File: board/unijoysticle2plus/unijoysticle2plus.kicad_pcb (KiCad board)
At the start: 2 copper layers, 4 parts, among them J1 DB9_Female, J2 DB9_Female, J4 Conn_01x02_Male, U1 ESP32-WROOM-32D

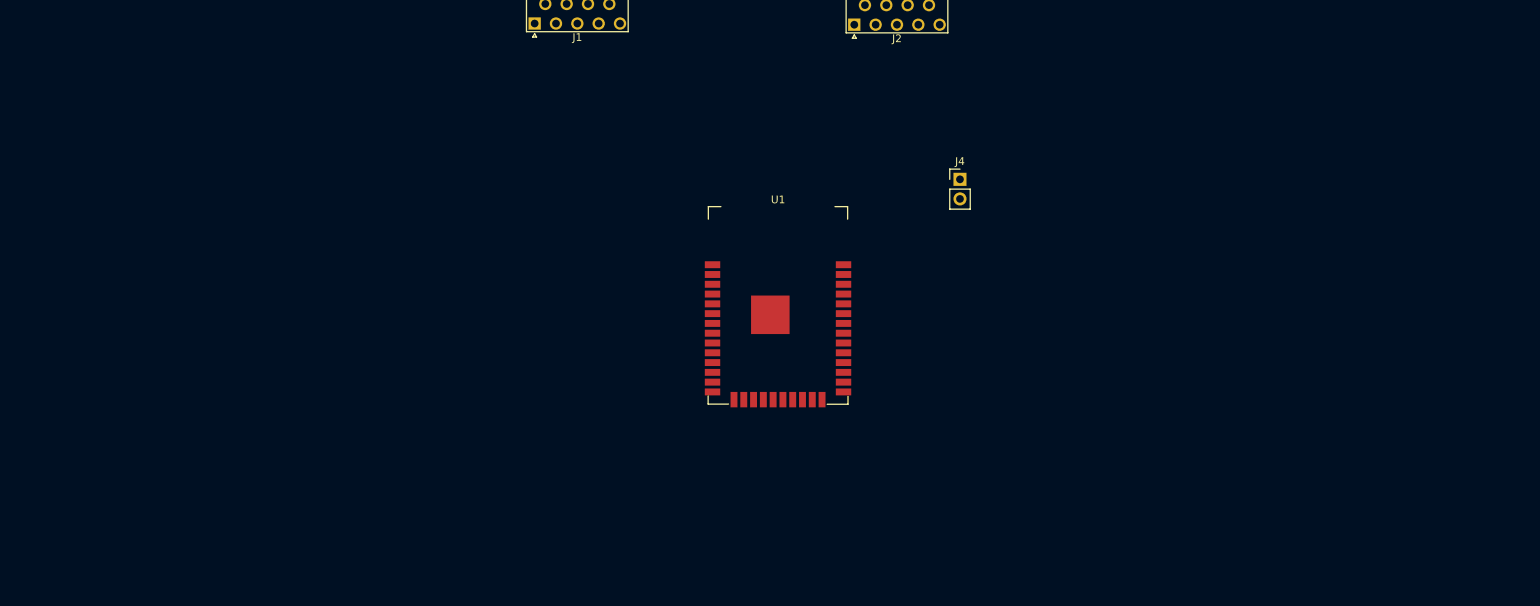
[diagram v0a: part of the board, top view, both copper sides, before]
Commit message: unijoysticle2plus: add some footprints
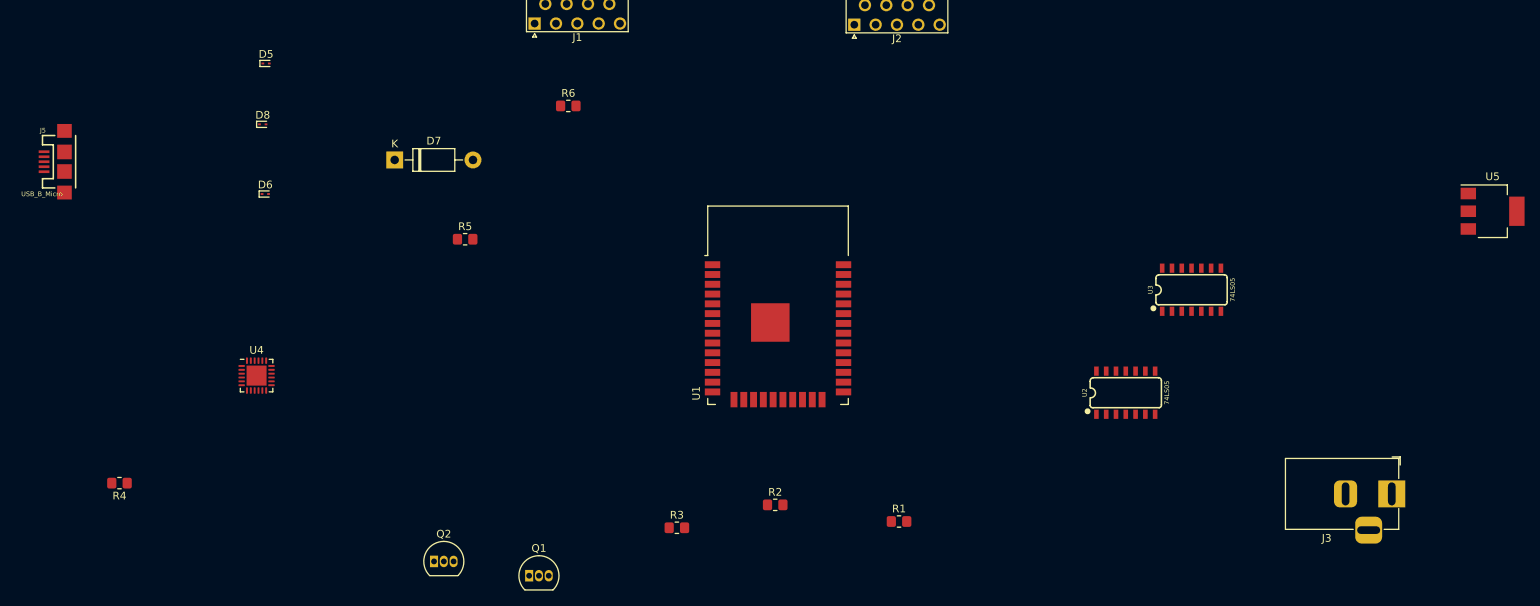
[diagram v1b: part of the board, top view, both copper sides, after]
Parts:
- removed J4: Conn_01x02_Male, Connector_PinHeader_2.54mm:PinHeader_1x02_P2.54mm_Vertical
- added D5: ESD9B5.0ST5G, Diode_SMD:D_SOD-923, F.Cu at (109.9, 81.0)
- added D6: ESD9B5.0ST5G, Diode_SMD:D_SOD-923, F.Cu at (109.8, 98.0)
- added D7: 1N5819, Diode_THT:D_DO-41_SOD81_P10.16mm_Horizontal, F.Cu at (126.5, 93.5)
- added D8: ESD9B5.0ST5G, Diode_SMD:D_SOD-923, F.Cu at (109.4, 88.9)
- added J3: Barrel_Jack, Connector_BarrelJack:BarrelJack_Horizontal, F.Cu at (255.9, 136.9)
- added J5: USB_B_Micro, Connectors:USB-MICROB, F.Cu at (83.7, 93.8)
- added Q1: S8050, Package_TO_SOT_THT:TO-92_Inline, F.Cu at (144.0, 147.5)
- added Q2: S8050, Package_TO_SOT_THT:TO-92_Inline, F.Cu at (131.6, 145.6)
- added R1: 150, Resistor_SMD:R_0805_2012Metric_Pad1.20x1.40mm_HandSolder, F.Cu at (192.0, 140.5)
- added R2: 150, Resistor_SMD:R_0805_2012Metric_Pad1.20x1.40mm_HandSolder, F.Cu at (175.9, 138.3)
- added R3: 10k, Resistor_SMD:R_0805_2012Metric_Pad1.20x1.40mm_HandSolder, F.Cu at (163.2, 141.3)
- added R4: 1k, Resistor_SMD:R_0805_2012Metric_Pad1.20x1.40mm_HandSolder, F.Cu at (90.8, 135.5)
- added R5: 10k, Resistor_SMD:R_0805_2012Metric_Pad1.20x1.40mm_HandSolder, F.Cu at (135.7, 103.8)
- added R6: 10k, Resistor_SMD:R_0805_2012Metric_Pad1.20x1.40mm_HandSolder, F.Cu at (149.1, 86.5)
- added U2: 74LS05, Silicon-Standard:SO14, F.Cu at (220.8, 123.7)
- added U3: 74LS05, Silicon-Standard:SO14, F.Cu at (229.3, 110.4)
- added U4: CP2102N-A01-GQFN24, Package_DFN_QFN:QFN-24-1EP_4x4mm_P0.5mm_EP2.6x2.6mm, F.Cu at (108.6, 121.5)
- added U5: AP2114H-3_3TRG1, Package_TO_SOT_SMD:SOT-223, F.Cu at (269.0, 100.2)
- U1: footprint digikey-footprints:ESP32-WROOM-32D -> RF_Module:ESP32-WROOM-32
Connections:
- net +5V renamed VDD
- J1 pad 1: (no net) -> /J1_UP
- J1 pad 2: (no net) -> /J1_DOWN
- J1 pad 3: (no net) -> /J1_LEFT
- J1 pad 4: (no net) -> /J1_RIGHT
- J1 pad 6: (no net) -> /J1_FIRE
- J2 pad 1: (no net) -> /J2_UP
- J2 pad 2: (no net) -> /J2_DOWN
- J2 pad 3: (no net) -> /J2_LEFT
- J2 pad 4: (no net) -> /J2_RIGHT
- J2 pad 6: (no net) -> /J2_FIRE
- U1 pad 10: (no net) -> /GPIO_J2_DOWN
- U1 pad 11: (no net) -> /GPIO_J1_UP
- U1 pad 12: (no net) -> /GPIO_J2_UP
- U1 pad 13: (no net) -> /GPIO_J1_FIRE
- U1 pad 14: (no net) -> /GPIO_J2_FIRE
- U1 pad 16: (no net) -> /GPIO_J2_LED
- U1 pad 2: (no net) -> +3V3
- U1 pad 28: (no net) -> /GPIO_J2_RIGHT
- U1 pad 29: (no net) -> /GPIO_J1_LED
- U1 pad 3: (no net) -> /RESET
- U1 pad 30: (no net) -> /GPIO_J1_DOWN
- U1 pad 31: (no net) -> /GPIO_J1_LEFT
- U1 pad 34: (no net) -> /RXD
- U1 pad 35: (no net) -> /TXD
- U1 pad 37: (no net) -> /GPIO_J1_RIGHT
- U1 pad 6: /GPIO34 -> (no net)
- U1 pad 7: /GPIO35 -> (no net)
- U1 pad 8: (no net) -> /GPIO_J2_LEFT

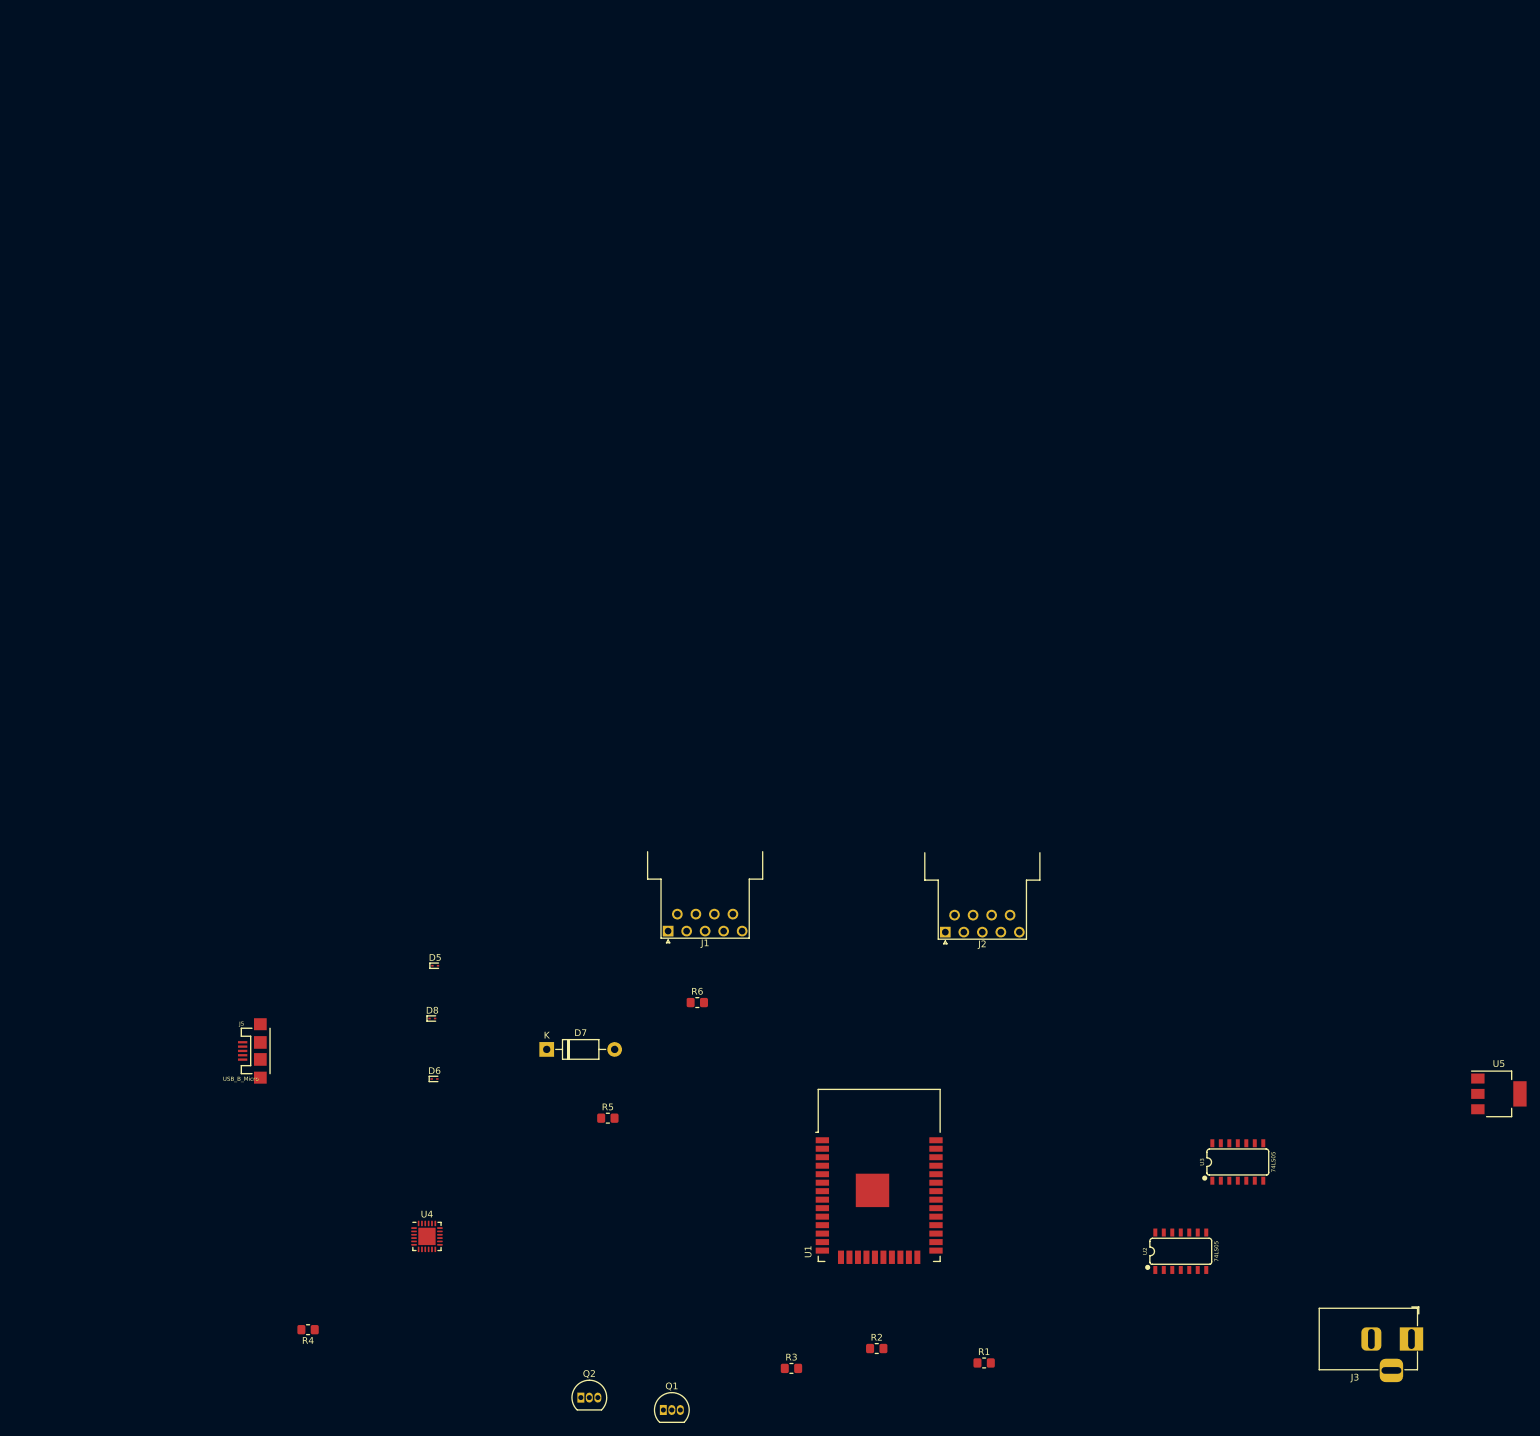
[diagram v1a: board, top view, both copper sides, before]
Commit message: unijoysticle2plus: more footprints
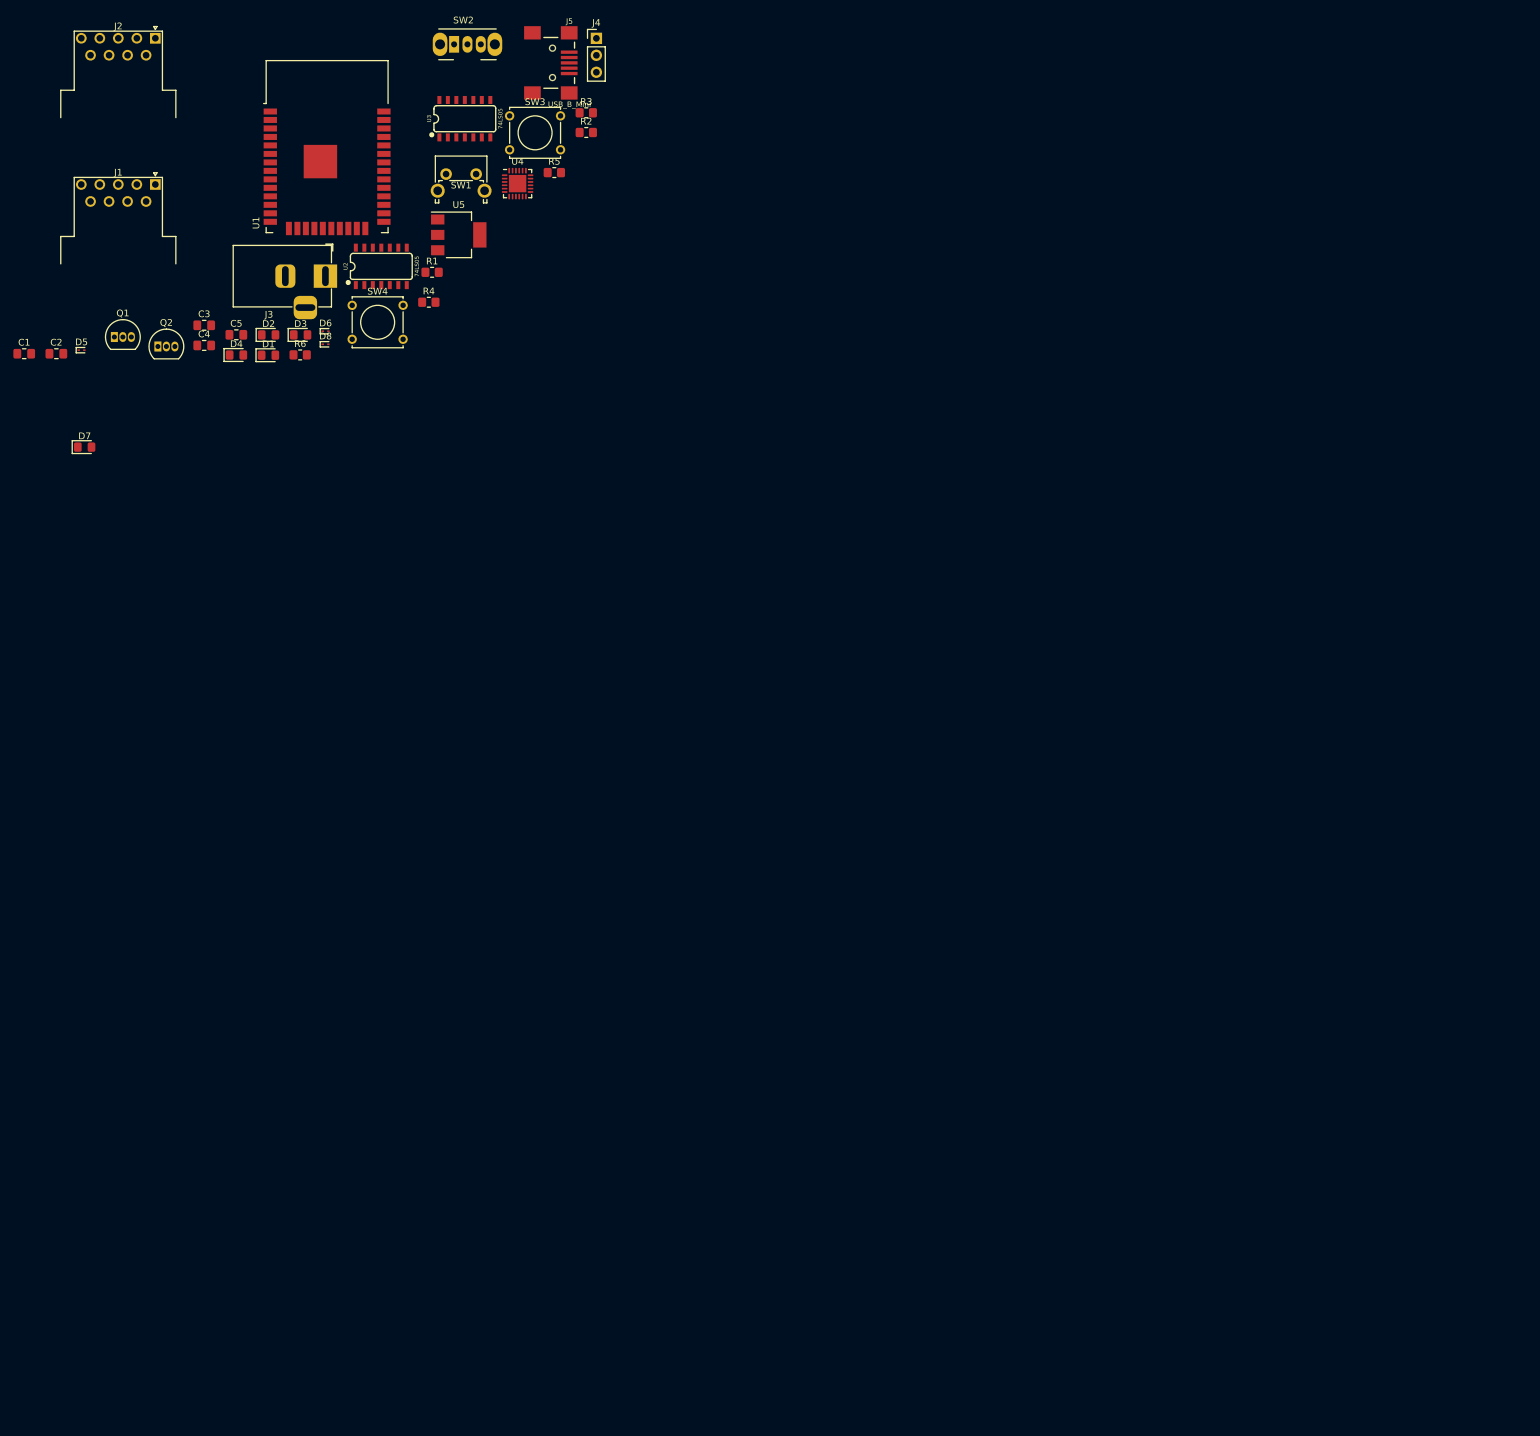
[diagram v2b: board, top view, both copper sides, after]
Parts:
- added C1: .1uF, Capacitor_SMD:C_0805_2012Metric_Pad1.18x1.45mm_HandSolder, F.Cu at (48.4, -10.5)
- added C2: 4.7uF, Capacitor_SMD:C_0805_2012Metric_Pad1.18x1.45mm_HandSolder, F.Cu at (53.2, -10.5)
- added C3: 0.1uF, Capacitor_SMD:C_0805_2012Metric_Pad1.18x1.45mm_HandSolder, F.Cu at (75.3, -14.8)
- added C4: 4.7uF, Capacitor_SMD:C_0805_2012Metric_Pad1.18x1.45mm_HandSolder, F.Cu at (75.3, -11.8)
- added C5: 4.7uF, Capacitor_SMD:C_0805_2012Metric_Pad1.18x1.45mm_HandSolder, F.Cu at (80.1, -13.4)
- added D1: LED, LED_SMD:LED_0805_2012Metric_Pad1.15x1.40mm_HandSolder, F.Cu at (84.9, -10.3)
- added D2: LED, LED_SMD:LED_0805_2012Metric_Pad1.15x1.40mm_HandSolder, F.Cu at (84.9, -13.4)
- added D3: 1N5819, Diode_SMD:D_0805_2012Metric_Pad1.15x1.40mm_HandSolder, F.Cu at (89.7, -13.4)
- added D4: 1N5819, Diode_SMD:D_0805_2012Metric_Pad1.15x1.40mm_HandSolder, F.Cu at (80.1, -10.4)
- added J4: Conn_01x03_Male, Connector_PinHeader_2.54mm:PinHeader_1x03_P2.54mm_Vertical, F.Cu at (134.0, -57.7)
- added SW1: SW_Push, Button_Switch_THT:SW_Tactile_SPST_Angled_PTS645Vx39-2LFS, F.Cu at (111.5, -37.4)
- added SW2: SW_SPST, Button_Switch_THT:SW_CuK_OS102011MA1QN1_SPDT_Angled, F.Cu at (112.7, -56.8)
- added SW3: SW_Push, Button_Switch_THT:SW_Tactile_Straight_KSA0Axx1LFTR, F.Cu at (121.0, -46.1)
- added SW4: SW_Push, Button_Switch_THT:SW_Tactile_Straight_KSA0Axx1LFTR, F.Cu at (97.4, -17.8)
- D7: footprint Diode_THT:D_DO-41_SOD81_P10.16mm_Horizontal -> Diode_SMD:D_0805_2012Metric_Pad1.15x1.40mm_HandSolder
- J5: value USB_B_Micro -> USB_B_Mini; footprint Connectors:USB-MICROB -> Connectors:USB-MINIB
- moved J3 227.4 mm to (93.4, -22.2)
- moved U5 201.8 mm to (113.4, -28.3)
- moved U3 194.3 mm to (113.7, -45.7)
- moved R3 190.4 mm to (132.5, -46.6)
- moved U2 189.8 mm to (101.2, -23.6)
- moved R2 187.1 mm to (132.5, -43.6)
- moved R1 182.9 mm to (109.4, -22.7)
- moved Q1 180.3 mm to (61.9, -13.0)
- moved J2 178.5 mm to (68.0, -57.7), turned to 0 degrees
- moved U1 174.7 mm to (93.7, -38.5)
- moved Q2 169.5 mm to (68.4, -11.6)
- moved U4 158.1 mm to (122.2, -36.0)
- moved R4 154.8 mm to (108.9, -18.2), turned to 0 degrees
- moved J5 154.2 mm to (127.4, -54.1)
- moved R5 141.7 mm to (127.7, -37.6)
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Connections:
- J3 pad 1: (no net) -> Net-(D3-Pad2)
- R1 pad 1: (no net) -> Net-(D1-Pad2)
- R2 pad 2: (no net) -> Net-(D2-Pad2)
- U1 pad 23: (no net) -> /GPIO_SWITCH_JOY
- U1 pad 25: (no net) -> Net-(SW4-Pad1)
- U1 pad 26: (no net) -> /GPIO04
- U1 pad 6: (no net) -> /GPIO34
- U1 pad 7: (no net) -> /GPIO35

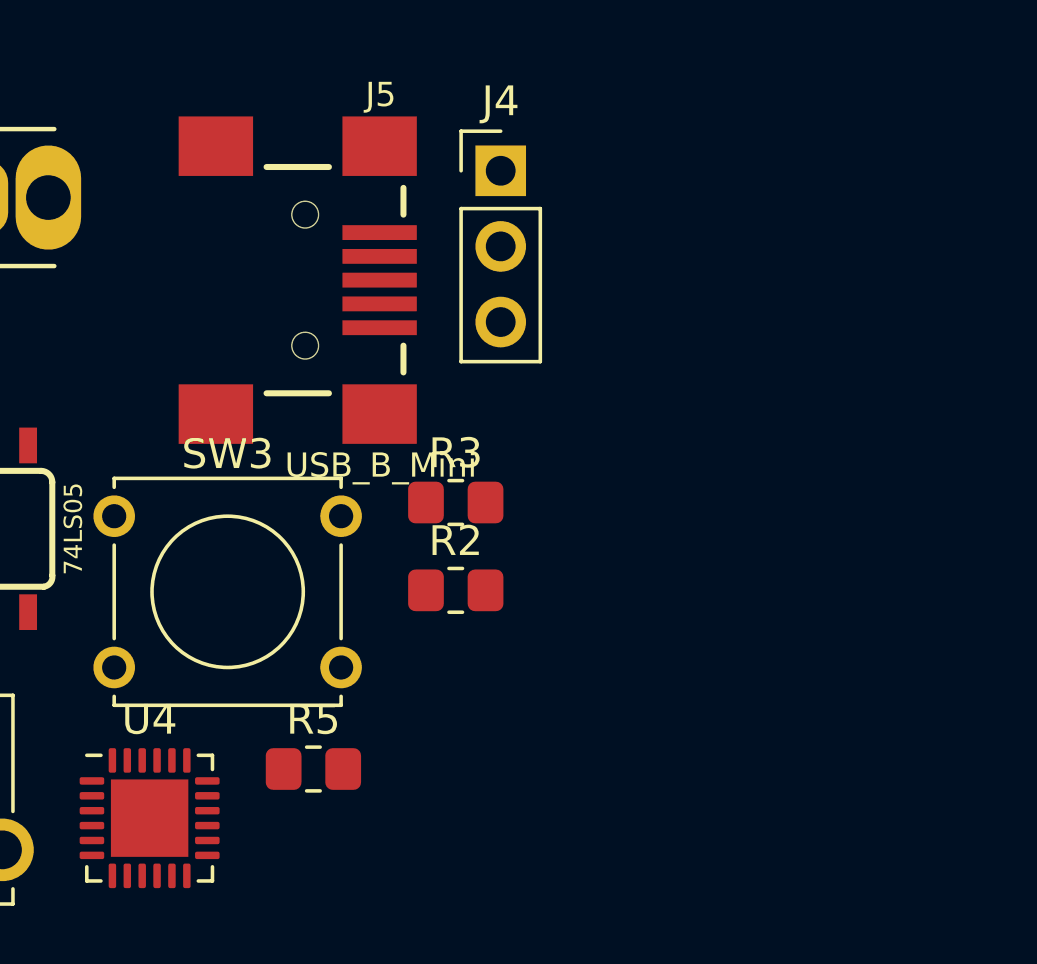
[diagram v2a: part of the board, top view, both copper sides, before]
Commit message: unijoysticle2plus: usb micro footprint connected
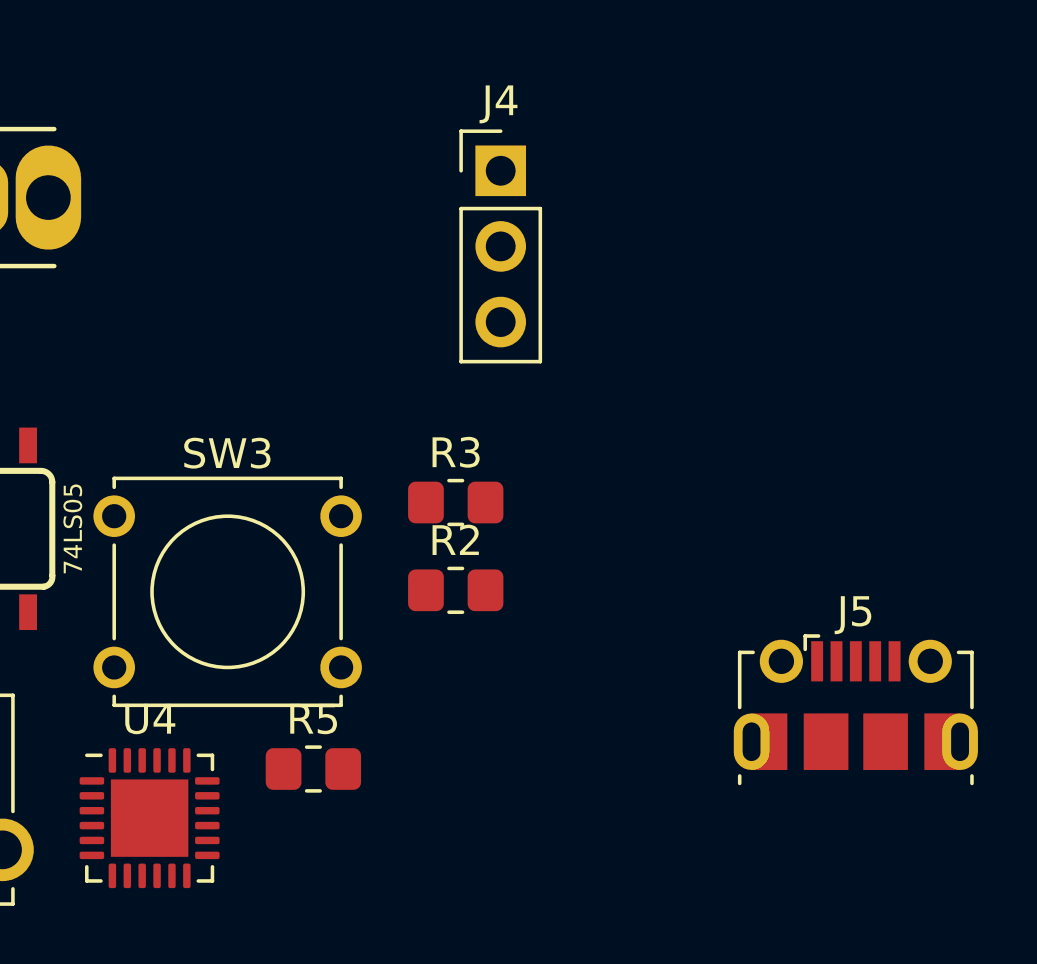
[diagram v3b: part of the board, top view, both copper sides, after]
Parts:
- J5: value USB_B_Mini -> USB_B_Micro; footprint Connectors:USB-MINIB -> Connector_USB:USB_Micro-B_Molex-105017-0001
- moved J5 23.4 mm to (145.9, -39.8)
